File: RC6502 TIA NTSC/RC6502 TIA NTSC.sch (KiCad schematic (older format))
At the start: 49 parts, among them J2 VDU_BASE, J4 Hole, J5 Hole, J6 Hole, J7 Hole, J8 Composite, U1 TIA_NTSC, U2 74HCT138, U3 VDU_Port, X1 3.579545 MHz

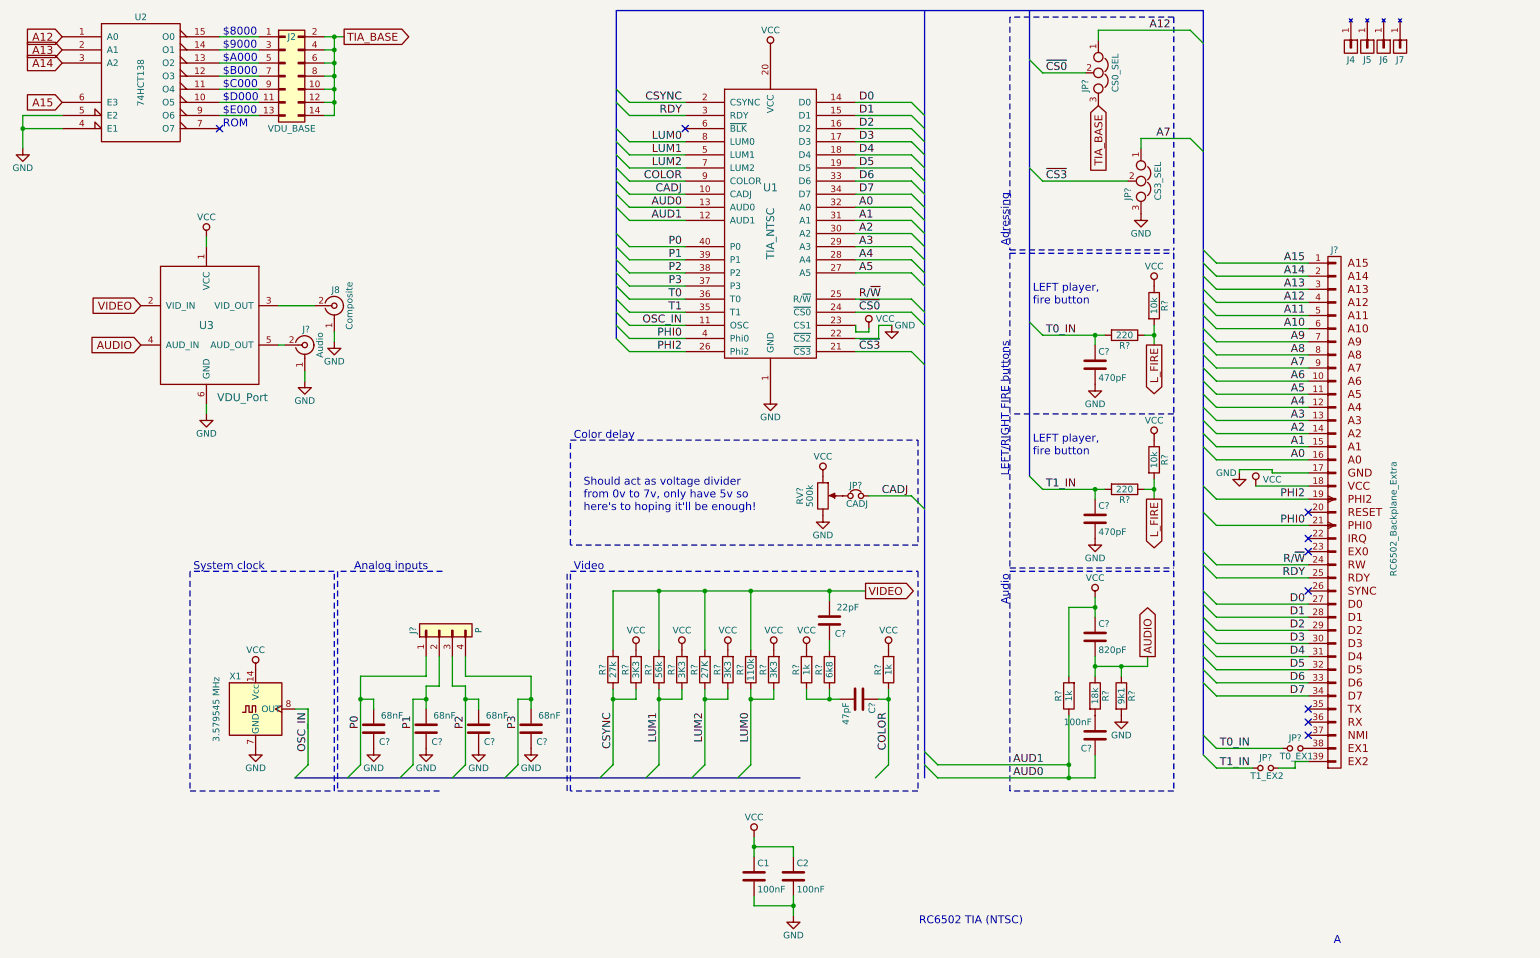
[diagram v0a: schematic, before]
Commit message: Assigned footprints
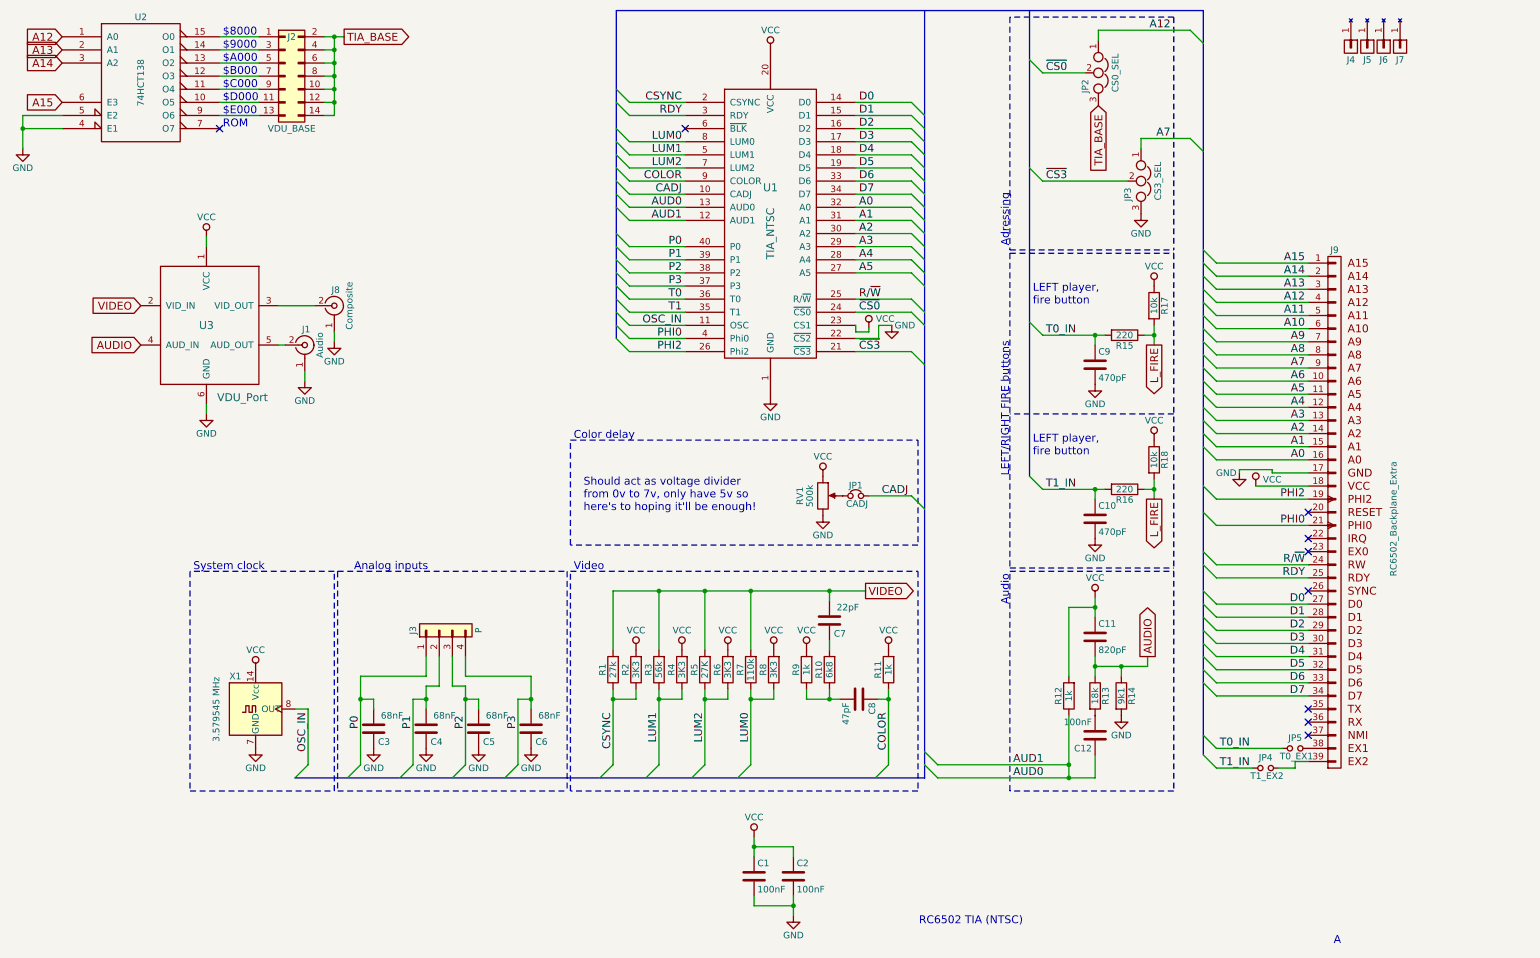
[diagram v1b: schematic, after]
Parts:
- J3: renamed from J?; footprint (none) -> Pin_Headers:Pin_Header_Straight_1x04_Pitch2.54mm
- J9: renamed from J?; footprint (none) -> Pin_Headers:Pin_Header_Angled_1x39_Pitch2.54mm
- JP1, JP4, JP5: renamed from JP?; footprint (none) -> Pin_Headers:Pin_Header_Straight_1x02_Pitch2.54mm
- JP2, JP3: renamed from JP?; footprint (none) -> Pin_Headers:Pin_Header_Straight_1x03_Pitch2.54mm
- R1, R10, R11, R12, R13, R14, R15, R16, R17, R18, R2, R3, R4, R5, R6, R7, R8, R9: renamed from R?; footprint (none) -> Resistors_THT:R_Axial_DIN0207_L6.3mm_D2.5mm_P10.16mm_Horizontal
- RV1: renamed from RV?; footprint (none) -> Potentiometers:Potentiometer_Trimmer_Bourns_3296W
- U1: footprint (none) -> Housings_DIP:DIP-40_W15.24mm_Socket
- gave numbers to parts that had none: 11

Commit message: TIA layout done
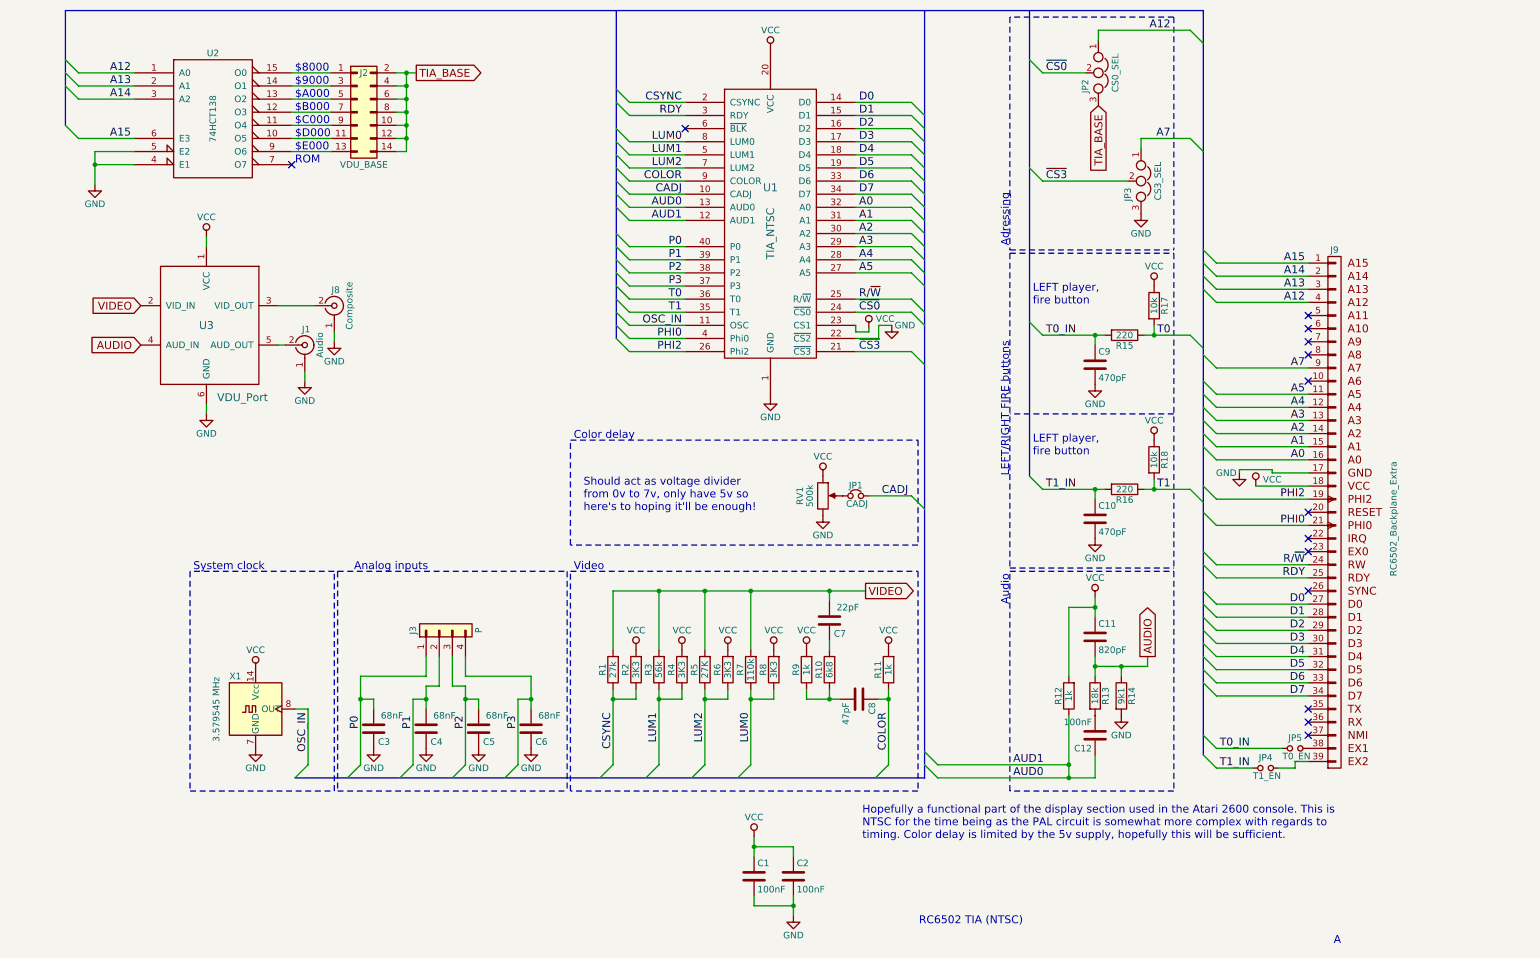
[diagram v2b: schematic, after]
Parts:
- removed J4, J5, J6, J7: Hole, mounting:Mounting, symbol Mounting
- J1, J8: footprint rca:rca_yellow -> RCA:rca_yellow
- JP4: value T1_EX2 -> T1_EN
- JP5: value T0_EX1 -> T0_EN
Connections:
- net T0: now also R15.1, R17.2
- net T1: now also R16.1, R18.2
- net A10: no longer names the net of J9.6 (A10)
- net A11: no longer names the net of J9.5 (A11)
- net A6: no longer names the net of J9.10 (A6)
- net A8: no longer names the net of J9.8 (A8)
- net A9: no longer names the net of J9.7 (A9)
- removed net L_FIRE: R15.1, R16.1, R17.2, R18.2
- no-connect marks 9 -> 14
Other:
- note added: "Hopefully a functional part of the display section used in the Atari 2600 console. This is\nNTSC for the time being as the PAL circuit is somewhat more complex with regards to\ntiming. Color delay is limited by the 5v supply, hopefully this will be sufficient."
- moved on the sheet: J2, U2
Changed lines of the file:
@@
 Comment4 ""
 $EndDescr
-Text GLabel 900  725  0    60   Input ~ 0
-A12
 Text Notes 8225 7500 2    60   ~ 0
 RC6502 TIA (NTSC)
@@
 L 74LS138 U2
 U 1 1 5C045924
-P 1500 1075
-F 0 "U2" H 1500 1575 50  0000 C CNN
-F 1 "74HCT138" V 1500 1075 50  0000 C CNN
-F 2 "Housings_DIP:DIP-16_W7.62mm_Socket" H 1500 1075 50  0001 C CNN
-F 3 "" H 1500 1075 50  0001 C CNN
-	1    1500 1075
-	1    0    0    -1
-$EndComp
-Text GLabel 900  825  0    60   Input ~ 0
-A13
-Text GLabel 900  925  0    60   Input ~ 0
-A14
-Text GLabel 900  1225 0    60   Input ~ 0
-A15
-Wire Wire Line
-	900  1325 600  1325
-Wire Wire Line
-	600  1325 600  1575
-Wire Wire Line
-	900  1425 600  1425
-Connection ~ 600  1425
+P 2050 1350
+F 0 "U2" H 2050 1850 50  0000 C CNN
+F 1 "74HCT138" V 2050 1350 50  0000 C CNN
+F 2 "Housings_DIP:DIP-16_W7.62mm_Socket" H 2050 1350 50  0001 C CNN
+F 3 "" H 2050 1350 50  0001 C CNN
+	1    2050 1350
+	1    0    0    -1
+$EndComp
+Wire Wire Line
+	1450 1600 1150 1600
+Wire Wire Line
+	1150 1600 1150 1850
+Wire Wire Line
+	1450 1700 1150 1700
+Connection ~ 1150 1700
 $Comp
 L Oscillator X1
@@
 	6175 7275 6175 7350
 $Comp
-L Mounting J4
-U 1 1 5C045951
-P 10725 800
-F 0 "J4" V 10825 800 50  0000 C CNN
-F 1 "Hole" V 10825 800 50  0001 C CNN
-F 2 "mounting:Mounting" H 10725 800 50  0001 C CNN
-F 3 "" H 10725 800 50  0001 C CNN
-	1    10725 800
-	0    1    1    0
-$EndComp
-$Comp
-L Mounting J6
-U 1 1 5C045952
-P 10975 800
-F 0 "J6" V 11075 800 50  0000 C CNN
-F 1 "Hole" V 11075 800 50  0001 C CNN
-F 2 "mounting:Mounting" H 10975 800 50  0001 C CNN
-F 3 "" H 10975 800 50  0001 C CNN
-	1    10975 800
-	0    1    1    0
-$EndComp
-$Comp
-L Mounting J5
-U 1 1 5C045953
-P 10850 800
-F 0 "J5" V 10950 800 50  0000 C CNN
-F 1 "Hole" V 10950 800 50  0001 C CNN
-F 2 "mounting:Mounting" H 10850 800 50  0001 C CNN
-F 3 "" H 10850 800 50  0001 C CNN
-	1    10850 800
-	0    1    1    0
-$EndComp
-$Comp
-L Mounting J7
-U 1 1 5C045954
-P 11100 800
-F 0 "J7" V 11200 800 50  0000 C CNN
-F 1 "Hole" V 11200 800 50  0001 C CNN
-F 2 "mounting:Mounting" H 11100 800 50  0001 C CNN
-F 3 "" H 11100 800 50  0001 C CNN
-	1    11100 800
-	0    1    1    0
-$EndComp
-$Comp
 L VCC #PWR01
 U 1 1 5C04B53B
@@
 L Conn_02x07_Odd_Even J2
 U 1 1 5C0413AA
-P 2600 1025
-F 0 "J2" H 2650 1325 50  0000 C CNN
-F 1 "VDU_BASE" H 2650 625 50  0000 C CNN
-F 2 "Pin_Headers:Pin_Header_Straight_2x07_Pitch2.54mm" H 2600 1025 50  0001 C CNN
-F 3 "" H 2600 1025 50  0001 C CNN
-	1    2600 1025
-	1    0    0    -1
-$EndComp
-Wire Wire Line
-	2100 725  2400 725
-Wire Wire Line
-	2100 825  2400 825
-Wire Wire Line
-	2100 925  2400 925
-Wire Wire Line
-	2100 1025 2400 1025
-Wire Wire Line
-	2100 1125 2400 1125
-NoConn ~ 2100 1425
-Wire Wire Line
-	2900 725  3050 725
-Wire Wire Line
-	2975 725  2975 1325
-Wire Wire Line
-	2975 1125 2900 1125
-Wire Wire Line
-	2900 1025 2975 1025
-Connection ~ 2975 1025
-Wire Wire Line
-	2900 925  2975 925
-Connection ~ 2975 925
-Wire Wire Line
-	2900 825  2975 825
-Connection ~ 2975 825
-Text Notes 2125 1425 0    60   ~ 0
+P 3150 1300
+F 0 "J2" H 3200 1600 50  0000 C CNN
+F 1 "VDU_BASE" H 3200 900 50  0000 C CNN
+F 2 "Pin_Headers:Pin_Header_Straight_2x07_Pitch2.54mm" H 3150 1300 50  0001 C CNN
+F 3 "" H 3150 1300 50  0001 C CNN
+	1    3150 1300
+	1    0    0    -1
+$EndComp
+Wire Wire Line
+	2650 1000 2950 1000
+Wire Wire Line
+	2650 1100 2950 1100
+Wire Wire Line
+	2650 1200 2950 1200
+Wire Wire Line
+	2650 1300 2950 1300
+Wire Wire Line
+	2650 1400 2950 1400
+NoConn ~ 2650 1700
+Wire Wire Line
+	3450 1000 3600 1000
+Wire Wire Line
+	3525 1000 3525 1600
+Wire Wire Line
+	3525 1400 3450 1400
+Wire Wire Line
+	3450 1300 3525 1300
+Connection ~ 3525 1300
+Wire Wire Line
+	3450 1200 3525 1200
+Connection ~ 3525 1200
+Wire Wire Line
+	3450 1100 3525 1100
+Connection ~ 3525 1100
+Text Notes 2675 1700 0    60   ~ 0
 ROM
-Text Notes 2125 1125 0    60   ~ 0
+Text Notes 2675 1400 0    60   ~ 0
 $C000
-Text Notes 2125 1025 0    60   ~ 0
+Text Notes 2675 1300 0    60   ~ 0
 $B000
-Text Notes 2125 925  0    60   ~ 0
+Text Notes 2675 1200 0    60   ~ 0
 $A000
-Text Notes 2125 825  0    60   ~ 0
+Text Notes 2675 1100 0    60   ~ 0
 $9000
-Text Notes 2125 725  0    60   ~ 0
+Text Notes 2675 1000 0    60   ~ 0
 $8000
-Connection ~ 2975 725
-Text GLabel 3050 725  2    60   Output ~ 0
+Connection ~ 3525 1000
+Text GLabel 3600 1000 2    60   Output ~ 0
 TIA_BASE
 $Comp
@@
 L GND #PWR06
 U 1 1 5C04D9C7
-P 600 1575
-F 0 "#PWR06" H 600 1325 50  0001 C CNN
-F 1 "GND" H 600 1425 50  0000 C CNN
-F 2 "" H 600 1575 50  0001 C CNN
-F 3 "" H 600 1575 50  0001 C CNN
-	1    600  1575
+P 1150 1850
+F 0 "#PWR06" H 1150 1600 50  0001 C CNN
+F 1 "GND" H 1150 1700 50  0000 C CNN
+F 2 "" H 1150 1850 50  0001 C CNN
+F 3 "" H 1150 1850 50  0001 C CNN
+	1    1150 1850
 	1    0    0    -1
 $EndComp
@@
 F 0 "J8" H 2985 2895 50  0000 C CNN
 F 1 "Composite" V 3090 2775 50  0000 C CNN
-F 2 "rca:rca_yellow" H 2975 2775 50  0001 C CNN
+F 2 "RCA:rca_yellow" H 2975 2775 50  0001 C CNN
 F 3 "" H 2975 2775 50  0001 C CNN
 	1    2975 2775
@@
 	2975 2975 2975 3050
 Wire Wire Line
-	2100 1225 2400 1225
-Wire Wire Line
-	2100 1325 2400 1325
-Text Notes 2125 1225 0    60   ~ 0
+	2650 1500 2950 1500
+Wire Wire Line
+	2650 1600 2950 1600
+Text Notes 2675 1500 0    60   ~ 0
 $D000
-Text Notes 2125 1325 0    60   ~ 0
+Text Notes 2675 1600 0    60   ~ 0
 $E000
 Wire Wire Line
-	2975 1225 2900 1225
-Connection ~ 2975 1125
-Wire Wire Line
-	2975 1325 2900 1325
-Connection ~ 2975 1225
+	3525 1500 3450 1500
+Connection ~ 3525 1400
+Wire Wire Line
+	3525 1600 3450 1600
+Connection ~ 3525 1500
 $Comp
 L RCA_PLUG J1
@@
 F 0 "J1" H 2760 3195 50  0000 C CNN
 F 1 "Audio" V 2865 3075 50  0000 C CNN
-F 2 "rca:rca_yellow" H 2750 3075 50  0001 C CNN
+F 2 "RCA:rca_yellow" H 2750 3075 50  0001 C CNN
 F 3 "" H 2750 3075 50  0001 C CNN
 	1    2750 3075
@@
 Text Label 10375 3450 2    60   ~ 0
 A5
-Text Label 10375 3350 2    60   ~ 0
-A6
 Text Label 10375 3250 2    60   ~ 0
 A7
-Text Label 10375 3150 2    60   ~ 0
-A8
-Text Label 10375 3050 2    60   ~ 0
-A9
-Text Label 10375 2950 2    60   ~ 0
-A10
-Text Label 10375 2850 2    60   ~ 0
-A11
 Text Label 10375 2750 2    60   ~ 0
 A12
@@
 	9700 3650 10400 3650
 Wire Wire Line
-	9700 3150 10400 3150
-Wire Wire Line
 	9700 3250 10400 3250
 Wire Wire Line
-	9700 3350 10400 3350
-Wire Wire Line
-	9700 2850 10400 2850
-Wire Wire Line
-	9700 2950 10400 2950
-Wire Wire Line
-	9700 3050 10400 3050
-Wire Wire Line
 	9700 2650 10400 2650
 Wire Wire Line
@@
 	9600 2650 9700 2750
 Entry Wire Line
-	9600 2750 9700 2850
-Entry Wire Line
-	9600 2850 9700 2950
-Entry Wire Line
-	9600 2950 9700 3050
-Entry Wire Line
-	9600 3050 9700 3150
-Entry Wire Line
 	9600 3150 9700 3250
-Entry Wire Line
-	9600 3250 9700 3350
 Entry Wire Line
 	9600 3350 9700 3450
@@
 P 10300 6150
 F 0 "JP5" H 10300 6230 50  0000 C CNN
-F 1 "T0_EX1" H 10310 6090 50  0000 C CNN
+F 1 "T0_EN" H 10310 6090 50  0000 C CNN
 F 2 "Pin_Headers:Pin_Header_Straight_1x02_Pitch2.54mm" H 10300 6150 50  0001 C CNN
 F 3 "" H 10300 6150 50  0001 C CNN
@@
 P 10075 6300
 F 0 "JP4" H 10075 6380 50  0000 C CNN
-F 1 "T1_EX2" H 10085 6240 50  0000 C CNN
+F 1 "T1_EN" H 10085 6240 50  0000 C CNN
 F 2 "Pin_Headers:Pin_Header_Straight_1x02_Pitch2.54mm" H 10075 6300 50  0001 C CNN
 F 3 "" H 10075 6300 50  0001 C CNN
@@
 Connection ~ 8775 3000
 Wire Wire Line
-	9150 3000 9225 3000
-Wire Wire Line
-	9225 2925 9225 3075
+	9150 3000 9500 3000
+Wire Wire Line
+	9225 2925 9225 3000
 $Comp
 L VCC #PWR020
@@
 $EndComp
 Connection ~ 9225 3000
-Text GLabel 9225 3075 3    60   Output ~ 0
-L_FIRE
 Entry Wire Line
 	8275 4075 8375 4175
@@
 Connection ~ 8775 4175
 Wire Wire Line
-	9150 4175 9225 4175
-Wire Wire Line
-	9225 4100 9225 4250
+	9150 4175 9500 4175
+Wire Wire Line
+	9225 4100 9225 4175
 $Comp
 L VCC #PWR022
@@
 $EndComp
 Connection ~ 9225 4175
-Text GLabel 9225 4250 3    60   Output ~ 0
-L_FIRE
 Text Notes 8300 2775 0    60   ~ 0
 LEFT player,\nfire button
@@
 	5125 525  5125 3025
 Wire Bus Line
-	5125 525  9600 525
+	925  525  9600 525
 Wire Wire Line
 	6475 7275 6475 7425
@@
 	3875 5675 3875 5450
 Connection ~ 3975 5775
+Text Notes 7000 6850 0    60   ~ 0
+Hopefully a functional part of the display section used in the Atari 2600 console. This is\nNTSC for the time being as the PAL circuit is somewhat more complex with regards to\ntiming. Color delay is limited by the 5v supply, hopefully this will be sufficient.
+Wire Wire Line
+	1450 1000 1025 1000
+Entry Wire Line
+	1025 1000 925  900
+Text Label 1425 1000 2    60   ~ 0
+A12
+Wire Wire Line
+	1450 1100 1025 1100
+Entry Wire Line
+	1025 1100 925  1000
+Text Label 1425 1100 2    60   ~ 0
+A13
+Wire Wire Line
+	1450 1200 1025 1200
+Entry Wire Line
+	1025 1200 925  1100
+Text Label 1425 1200 2    60   ~ 0
+A14
+Wire Wire Line
+	1450 1500 1025 1500
+Entry Wire Line
+	1025 1500 925  1400
+Text Label 1425 1500 2    60   ~ 0
+A15
+Wire Bus Line
+	925  525  925  1400
+Entry Wire Line
+	9500 3000 9600 3100
+Entry Wire Line
+	9500 4175 9600 4275
+Text Label 9350 3000 2    60   ~ 0
+T0
+Text Label 9350 4175 2    60   ~ 0
+T1
+NoConn ~ 10400 2850
+NoConn ~ 10400 2950
+NoConn ~ 10400 3050
+NoConn ~ 10400 3150
+NoConn ~ 10400 3350
 $EndSCHEMATC

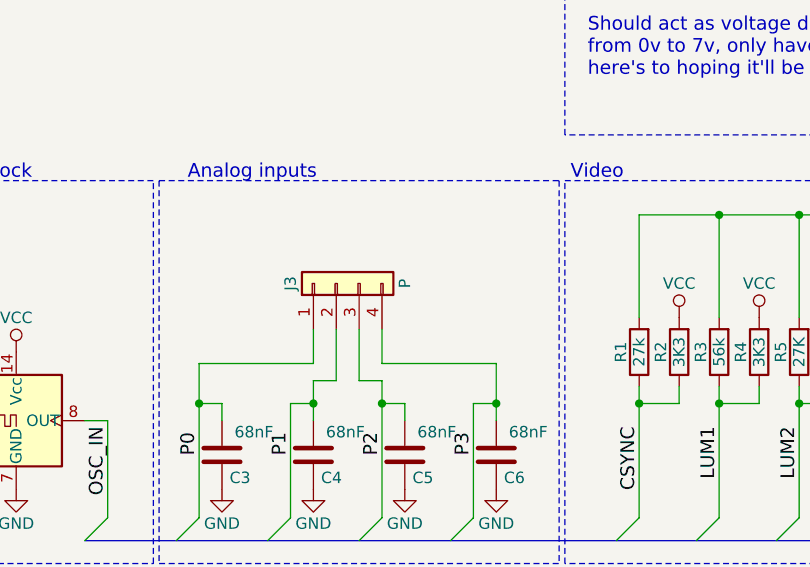
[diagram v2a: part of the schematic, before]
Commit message: Renamed P to analog to match RIOT
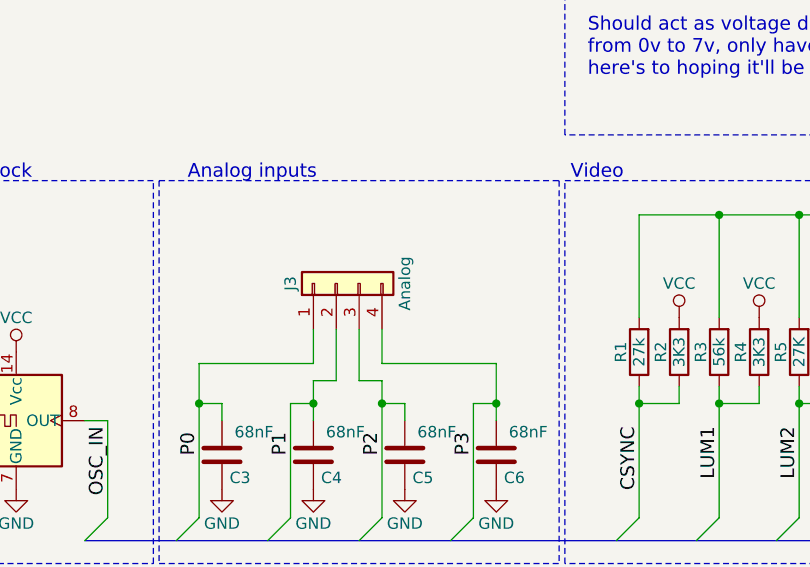
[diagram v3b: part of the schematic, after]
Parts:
- J3: value P -> Analog
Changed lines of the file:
@@
 P 3775 5250
 F 0 "J3" H 3775 5450 50  0000 C CNN
-F 1 "P" H 3775 4950 50  0000 C CNN
+F 1 "Analog" H 3775 4950 50  0000 C CNN
 F 2 "Pin_Headers:Pin_Header_Straight_1x04_Pitch2.54mm" H 3775 5250 50  0001 C CNN
 F 3 "" H 3775 5250 50  0001 C CNN
